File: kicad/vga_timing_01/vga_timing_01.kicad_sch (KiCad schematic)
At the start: 13 parts, among them J1 DIN41612_02x32_AC, J2 UART1, J3 UART2, U10 TL28L92FR, U13 74AHC1G32, Y1 Crystal 3.6864MHz

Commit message: vga timing board 01 work
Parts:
- removed C1, C2: 100nF, Capacitor_THT:C_Disc_D4.7mm_W2.5mm_P5.00mm, symbol Device:C
- removed J1: DIN41612_02x32_AC, Connector_DIN:DIN41612_C_2x32_Male_Horizontal_THT, symbol Connector:DIN41612_02x32_AC
- removed J2: UART1, Connector_PinHeader_2.54mm:PinHeader_2x03_P2.54mm_Horizontal, symbol Connector_Generic:Conn_02x03_Odd_Even
- removed J3: UART2, Connector_PinHeader_2.54mm:PinHeader_2x03_P2.54mm_Horizontal, symbol Connector_Generic:Conn_02x03_Odd_Even
- removed JP1, JP2: SolderJumper_3_Open, Jumper:SolderJumper-3_P1.3mm_Open_RoundedPad1.0x1.5mm_NumberLabels, symbol Jumper:SolderJumper_3_Open
- removed U10: TL28L92FR, Package_QFP:MQFP-44_10x10mm_P0.8mm, symbol 2024-09-25_17-04-06:TL28L92FR
- removed U13: 74AHC1G32, Package_TO_SOT_SMD:SOT-23-5_HandSoldering, symbol 74xGxx:74AHC1G32
- removed Y1: Crystal 3.6864MHz, Crystal:Crystal_HC49-4H_Vertical, symbol Device:Crystal
- added J1: Conn_02x01, Connector_PinSocket_1.27mm:PinSocket_2x01_P1.27mm_Vertical, symbol Connector_Generic:Conn_02x01
- added U1, U2, U3: 74LS393, Package_SO:SOIC-14_3.9x8.7mm_P1.27mm, symbol 74xx:74LS393
- added U4, U5: PAL20RS10, Package_DIP:DIP-24_W7.62mm_Socket, symbol Logic_Programmable:PAL20RS10
- added X1: ACO-14MHz, Package_DIP:DIP-14_W7.62mm_Socket, symbol 65xx:osci-14or8
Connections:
- net CLOCK: now also U1.1 (CP), U4.1 (CLK), U5.1 (CLK), X1.8 (OUT)
- net GND: now also J1.1 (Pin_1), U1.7 (GND), U2.7 (GND), U3.7 (GND), U4.12 (GND), U4.13 (~{OE}), U5.12 (GND), U5.13 (~{OE}), X1.7 (GND)
- net VCC: now also J1.2 (Pin_2), U1.14 (VCC), U2.14 (VCC), U3.14 (VCC), U4.24 (VCC), U5.24 (VCC), X1.11 (Vcc), X1.14 (Vcc)
- new net H00: U1.3 (Q0), U4.2 (I0)
- new net H01: U1.4 (Q1), U4.3 (I1)
- new net H02: U1.5 (Q2), U4.4 (I2)
- new net H03: U1.13 (CP), U1.6 (Q3), U4.5 (I3)
- new net H04: U1.11 (Q0), U4.6 (I4)
- new net H05: U1.10 (Q1), U4.7 (I5)
- new net H06: U1.9 (Q2), U4.8 (I6)
- new net H07: U1.8 (Q3), U2.1 (CP), U4.9 (I7)
- new net H08: U2.3 (Q0), U4.10 (I8)
- new net H09: U2.4 (Q1), U4.11 (I9)
- new net H10: U2.5 (Q2)
- new net H11: U2.6 (Q3)
- new net H_SYNC: U4.22 (O1)
- new net V00: U2.11 (Q0), U5.2 (I0)
- new net V01: U2.10 (Q1), U5.3 (I1)
- new net V02: U2.9 (Q2), U5.4 (I2)
- new net V03: U2.8 (Q3), U3.1 (CP), U5.5 (I3)
- new net V04: U3.3 (Q0), U5.6 (I4)
- new net V05: U3.4 (Q1), U5.7 (I5)
- new net V06: U3.5 (Q2), U5.8 (I6)
- new net V07: U3.13 (CP), U3.6 (Q3), U5.9 (I7)
- new net V08: U3.11 (Q0), U5.10 (I8)
- new net V09: U3.10 (Q1), U5.11 (I9)
- new net V10: U3.9 (Q2)
- new net V11: U3.8 (Q3)
- new net V_SYNC: U5.22 (O1)
- new net ~{H_RES}: U1.12 (MR), U1.2 (MR), U2.13 (CP), U2.2 (MR), U4.23 (O0)
- new net ~{V_RES}: U2.12 (MR), U3.12 (MR), U3.2 (MR), U5.23 (O0)
- no-connect marks 23 -> 0

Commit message: test kicad busses
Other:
- moved on the sheet: C3, C4, C5, U1A, U1B, U2A, U2B, U3A, U3B, U4, U5

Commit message: routing improvements
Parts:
- U1, U2, U3: footprint Package_SO:SOIC-14_3.9x8.7mm_P1.27mm -> Package_SO:SO-14_3.9x8.65mm_P1.27mm
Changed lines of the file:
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@@
 			)
 		)
-		(property "Footprint" "Package_SO:SOIC-14_3.9x8.7mm_P1.27mm"
+		(property "Footprint" "Package_SO:SO-14_3.9x8.65mm_P1.27mm"
 			(at 106.68 33.02 0)
 			(effects
@@
 			)
 		)
-		(property "Footprint" "Package_SO:SOIC-14_3.9x8.7mm_P1.27mm"
+		(property "Footprint" "Package_SO:SO-14_3.9x8.65mm_P1.27mm"
 			(at 181.61 67.31 0)
 			(effects
@@
 			)
 		)
-		(property "Footprint" "Package_SO:SOIC-14_3.9x8.7mm_P1.27mm"
+		(property "Footprint" "Package_SO:SO-14_3.9x8.65mm_P1.27mm"
 			(at 181.61 113.03 0)
 			(effects
@@
 			)
 		)
-		(property "Footprint" "Package_SO:SOIC-14_3.9x8.7mm_P1.27mm"
+		(property "Footprint" "Package_SO:SO-14_3.9x8.65mm_P1.27mm"
 			(at 181.61 29.21 0)
 			(effects
@@
 			)
 		)
-		(property "Footprint" "Package_SO:SOIC-14_3.9x8.7mm_P1.27mm"
+		(property "Footprint" "Package_SO:SO-14_3.9x8.65mm_P1.27mm"
 			(at 86.36 33.02 0)
 			(effects
@@
 			)
 		)
-		(property "Footprint" "Package_SO:SOIC-14_3.9x8.7mm_P1.27mm"
+		(property "Footprint" "Package_SO:SO-14_3.9x8.65mm_P1.27mm"
 			(at 181.61 93.98 0)
 			(effects
@@
 			)
 		)
-		(property "Footprint" "Package_SO:SOIC-14_3.9x8.7mm_P1.27mm"
+		(property "Footprint" "Package_SO:SO-14_3.9x8.65mm_P1.27mm"
 			(at 181.61 132.08 0)
 			(effects
@@
 			)
 		)
-		(property "Footprint" "Package_SO:SOIC-14_3.9x8.7mm_P1.27mm"
+		(property "Footprint" "Package_SO:SO-14_3.9x8.65mm_P1.27mm"
 			(at 127 33.02 0)
 			(effects
@@
 			)
 		)
-		(property "Footprint" "Package_SO:SOIC-14_3.9x8.7mm_P1.27mm"
+		(property "Footprint" "Package_SO:SO-14_3.9x8.65mm_P1.27mm"
 			(at 181.61 48.26 0)
 			(effects

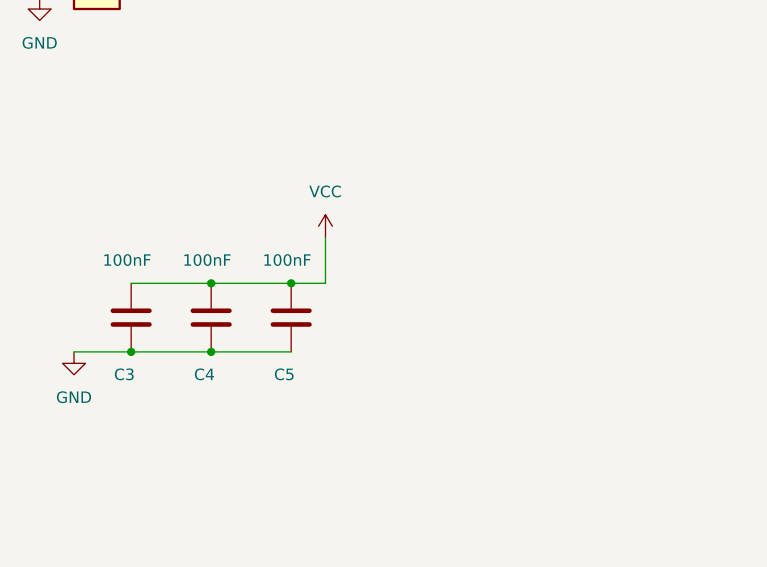
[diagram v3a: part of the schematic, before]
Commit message: WIP vga timing
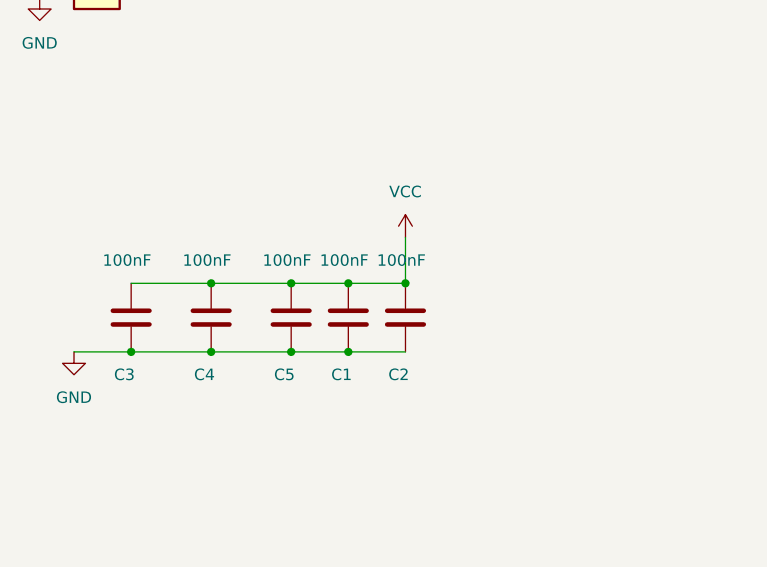
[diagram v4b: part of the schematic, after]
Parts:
- added C1, C2: 100nF, Capacitor_SMD:C_0805_2012Metric_Pad1.18x1.45mm_HandSolder, symbol Device:C
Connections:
- net GND: now also C1.2, C2.2
- net VCC: now also C1.1, C2.1
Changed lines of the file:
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@@
 	)
 	(junction
+		(at 62.23 95.25)
+		(diameter 0)
+		(color 0 0 0 0)
+	)
+	(junction
 		(at 194.31 53.34)
 		(diameter 0)
@@
 	)
 	(junction
+		(at 55.88 102.87)
+		(diameter 0)
+		(color 0 0 0 0)
+	)
+	(junction
+		(at 62.23 102.87)
+		(diameter 0)
+		(color 0 0 0 0)
+	)
+	(junction
 		(at 106.68 45.72)
 		(diameter 0)
@@
 		(color 0 0 0 0)
 	)
+	(junction
+		(at 68.58 95.25)
+		(diameter 0)
+		(color 0 0 0 0)
+	)
 	(bus_entry
 		(at 198.12 50.8)
@@
 	(wire
 		(pts
-			(xy 59.69 90.17) (xy 59.69 95.25)
+			(xy 68.58 90.17) (xy 68.58 95.25)
 		)
 		(stroke
@@
 		)
 	)
+	(wire
+		(pts
+			(xy 55.88 102.87) (xy 62.23 102.87)
+		)
+		(stroke
+			(width 0)
+			(type default)
+		)
+	)
 	(bus
 		(pts
@@
 	(wire
 		(pts
+			(xy 62.23 95.25) (xy 68.58 95.25)
+		)
+		(stroke
+			(width 0)
+			(type default)
+		)
+	)
+	(wire
+		(pts
 			(xy 106.68 20.32) (xy 127 20.32)
 		)
@@
 	(wire
 		(pts
-			(xy 59.69 95.25) (xy 55.88 95.25)
+			(xy 55.88 95.25) (xy 62.23 95.25)
 		)
 		(stroke
@@
 	(wire
 		(pts
+			(xy 62.23 102.87) (xy 68.58 102.87)
+		)
+		(stroke
+			(width 0)
+			(type default)
+		)
+	)
+	(wire
+		(pts
 			(xy 214.63 54.61) (xy 210.82 54.61)
 		)
@@
 	)
 	(symbol
+		(lib_id "Device:C")
+		(at 62.23 99.06 0)
+		(unit 1)
+		(exclude_from_sim no)
+		(in_bom yes)
+		(on_board yes)
+		(dnp no)
+		(property "Reference" "C1"
+			(at 60.325 105.41 0)
+			(effects
+				(font
+					(size 1.27 1.27)
+				)
+				(justify left)
+			)
+		)
+		(property "Value" "100nF"
+			(at 59.055 92.71 0)
+			(effects
+				(font
+					(size 1.27 1.27)
+				)
+				(justify left)
+			)
+		)
+		(property "Footprint" "Capacitor_SMD:C_0805_2012Metric_Pad1.18x1.45mm_HandSolder"
+			(at 63.1952 102.87 0)
+			(effects
+				(font
+					(size 1.27 1.27)
+				)
+				(hide yes)
+			)
+		)
+		(property "Datasheet" "~"
+			(at 62.23 99.06 0)
+			(effects
+				(font
+					(size 1.27 1.27)
+				)
+				(hide yes)
+			)
+		)
+		(property "Description" ""
+			(at 62.23 99.06 0)
+			(effects
+				(font
+					(size 1.27 1.27)
+				)
+			)
+		)
+		(pin "1"
+		)
+		(pin "2"
+		)
+		(instances
+			(project "vga_timing_01"
+				(path "/cb13e431-64f0-4016-a936-ee98aca3391f"
+					(reference "C1")
+					(unit 1)
+				)
+			)
+		)
+	)
+	(symbol
 		(lib_name "VCC_1")
 		(lib_id "power:VCC")
@@
 	(symbol
 		(lib_id "power:VCC")
-		(at 59.69 90.17 0)
+		(at 68.58 90.17 0)
 		(unit 1)
 		(exclude_from_sim no)
@@
 		(dnp no)
 		(property "Reference" "#PWR040"
-			(at 59.69 93.98 0)
+			(at 68.58 93.98 0)
 			(effects
 				(font
@@
 		)
 		(property "Value" "VCC"
-			(at 59.69 85.09 0)
+			(at 68.58 85.09 0)
 			(effects
 				(font
@@
 		)
 		(property "Footprint" ""
-			(at 59.69 90.17 0)
+			(at 68.58 90.17 0)
 			(effects
 				(font
@@
 		)
 		(property "Datasheet" ""
-			(at 59.69 90.17 0)
+			(at 68.58 90.17 0)
 			(effects
 				(font
@@
 		)
 		(property "Description" ""
-			(at 59.69 90.17 0)
+			(at 68.58 90.17 0)
 			(effects
 				(font
@@
 					(unit 1)
 				)
+			)
+		)
+	)
+	(symbol
+		(lib_id "Device:C")
+		(at 68.58 99.06 0)
+		(unit 1)
+		(exclude_from_sim no)
+		(in_bom yes)
+		(on_board yes)
+		(dnp no)
+		(property "Reference" "C2"
+			(at 66.675 105.41 0)
+			(effects
+				(font
+					(size 1.27 1.27)
+				)
+				(justify left)
+			)
+		)
+		(property "Value" "100nF"
+			(at 65.405 92.71 0)
+			(effects
+				(font
+					(size 1.27 1.27)
+				)
+				(justify left)
+			)
+		)
+		(property "Footprint" "Capacitor_SMD:C_0805_2012Metric_Pad1.18x1.45mm_HandSolder"
+			(at 69.5452 102.87 0)
+			(effects
+				(font
+					(size 1.27 1.27)
+				)
+				(hide yes)
+			)
+		)
+		(property "Datasheet" "~"
+			(at 68.58 99.06 0)
+			(effects
+				(font
+					(size 1.27 1.27)
+				)
+				(hide yes)
+			)
+		)
+		(property "Description" ""
+			(at 68.58 99.06 0)
+			(effects
+				(font
+					(size 1.27 1.27)
+				)
+			)
+		)
+		(pin "1"
+		)
+		(pin "2"
+		)
+		(instances
+			(project "vga_timing_01"
+				(path "/cb13e431-64f0-4016-a936-ee98aca3391f"
+					(reference "C2")
+					(unit 1)
+				)
